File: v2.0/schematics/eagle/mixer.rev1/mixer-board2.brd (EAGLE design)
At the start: 100 x 80 mm, 70 parts, among them IC1 TL084P, IC2 TL084P, IC3 TL082P

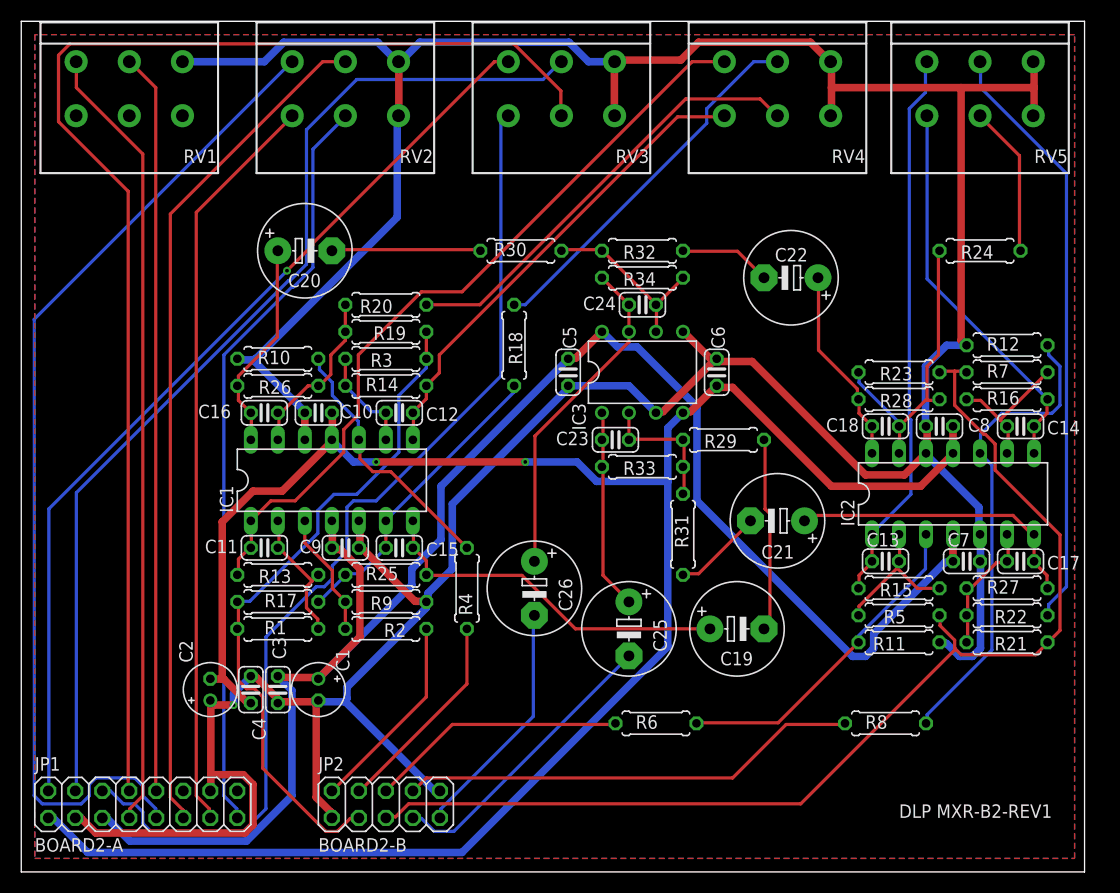
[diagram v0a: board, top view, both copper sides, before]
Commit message: Mixer Board 3 layout
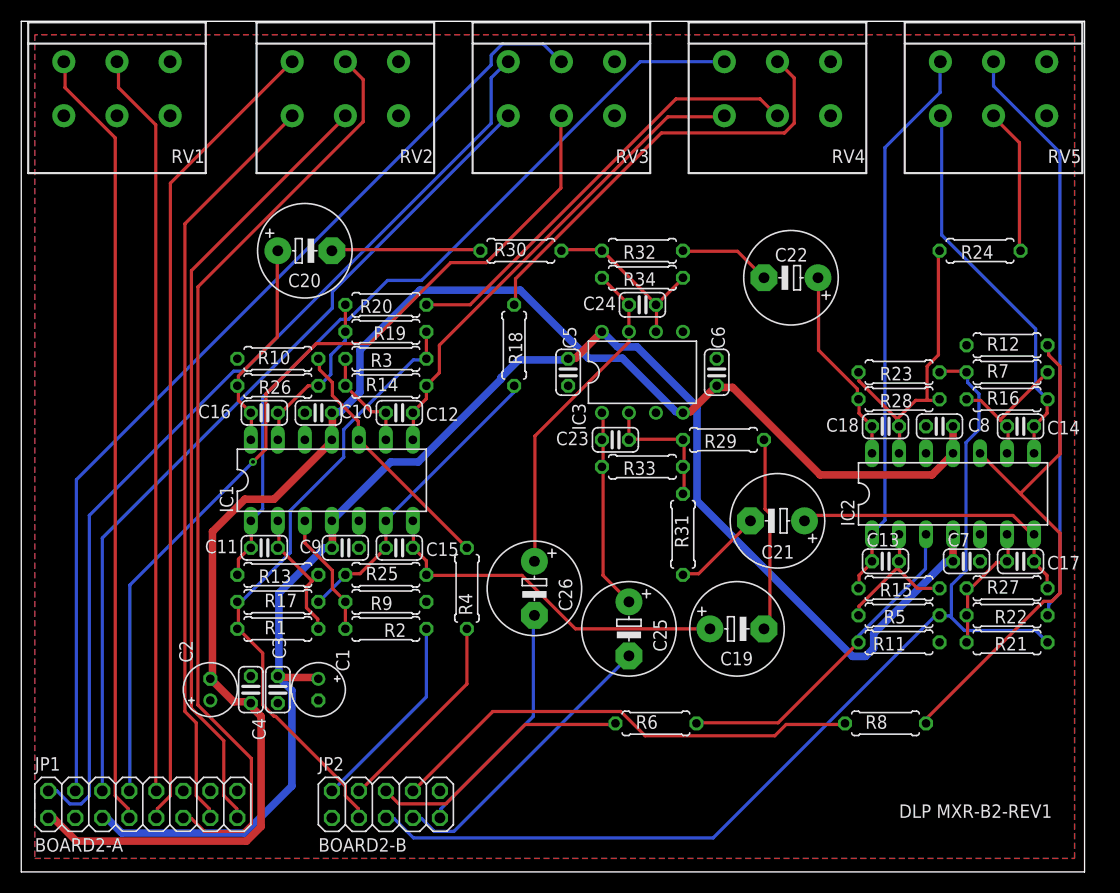
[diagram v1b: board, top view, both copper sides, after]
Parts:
- moved RV5 1.27 mm to (91.4, 76.2)
- moved RV1 1.16 mm to (9.00, 76.2)
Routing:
- net 0V: track 378.2 -> 0.00 mm, vias 1 -> 0
- net -12V: track 193.3 -> 147.8 mm, vias 2 -> 0
- net ST2-LVL-5: track 123.9 -> 85.3 mm, vias 0 -> 1
- net ST1-LVL-3: track 95.1 -> 76.4 mm
- net ST2-LVL-6: track 94.8 -> 79.3 mm
- net +12V: track 156.2 -> 143.1 mm
- net ST1-LVL-2: track 79.7 -> 88.1 mm
- net N$2: track 35.0 -> 41.3 mm
- net FX2-SEND: track 106.3 -> 100.0 mm
- net N$29: track 45.0 -> 50.2 mm
- net FX1-SEND: track 63.9 -> 58.9 mm
- net ST2-LVL-2: track 98.0 -> 93.2 mm
- net ST2-LVL-3: track 87.3 -> 90.6 mm, vias 1 -> 0
- net ST1-LVL-5: track 71.4 -> 73.8 mm
- net FX2-RTN-R: track 43.3 -> 45.2 mm
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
